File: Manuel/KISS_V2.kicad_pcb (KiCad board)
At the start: 4 copper layers, 127.4 x 127.4 mm, 73 parts, among them J1 Screw_Terminal_01x03, J2 Screw_Terminal_01x02, J3 Screw_Terminal_01x02, J5 Screw_Terminal_01x02, Q1 BC817, U1 MQ-6, U2 ULN2003, U3 AMS1117-3.3, U4 AMS1117-5.0, U5 ULN2003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

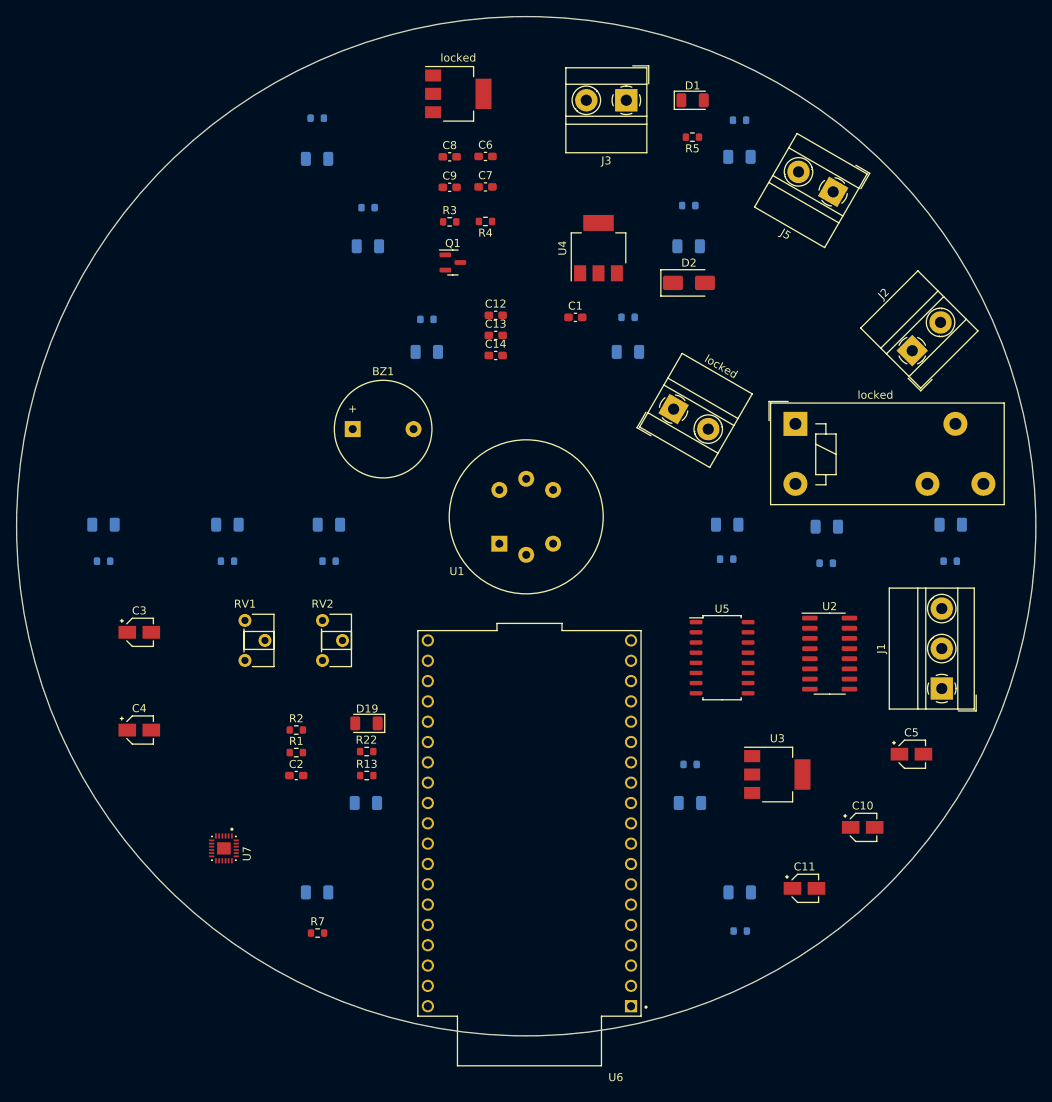
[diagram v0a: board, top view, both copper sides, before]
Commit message: Proyecto Kiss V2
Esquemático y PCB terminados
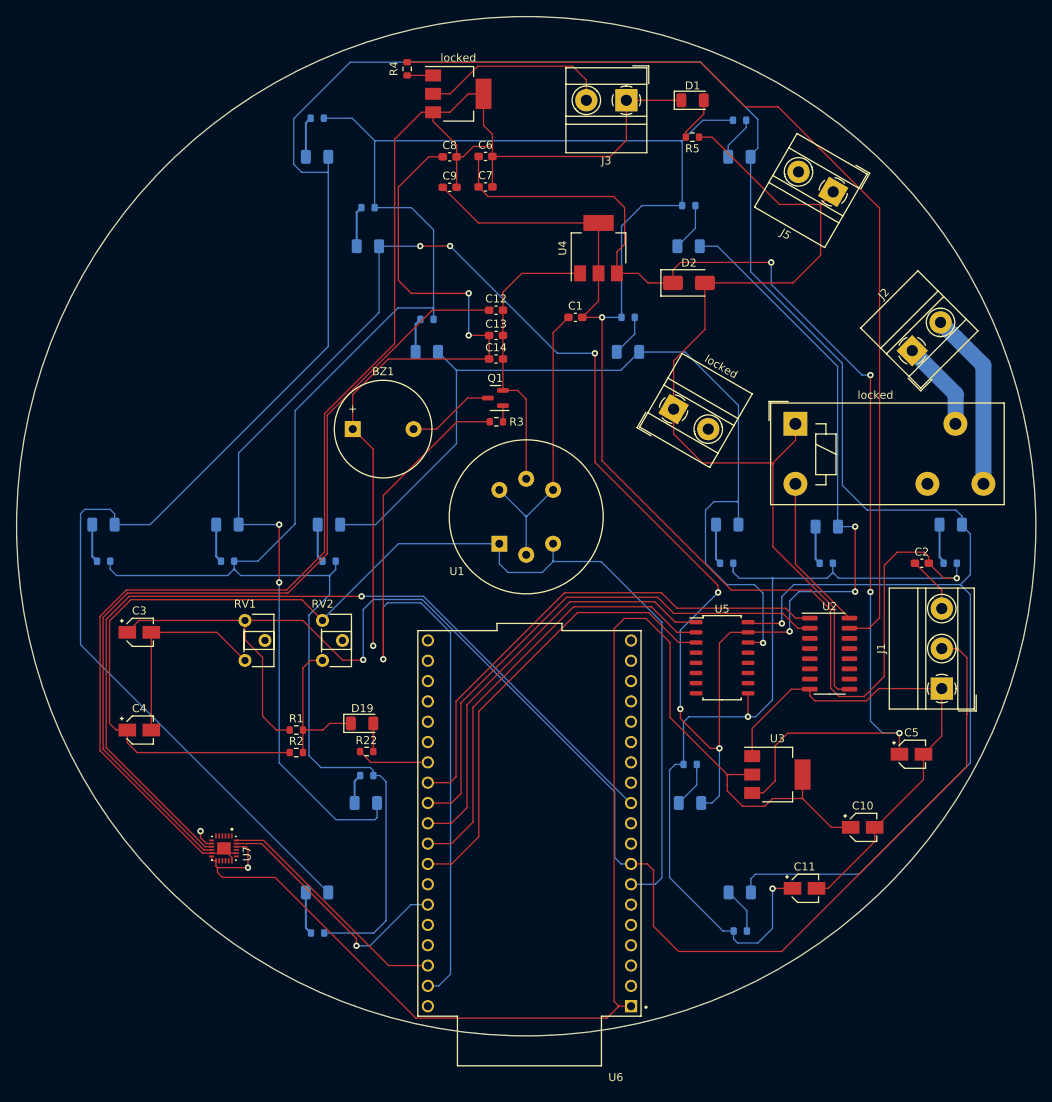
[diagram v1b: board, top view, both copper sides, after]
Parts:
- R13, R7: moved to B.Cu
- RV1, RV2: value 60K -> 20K
- moved R10 96.7 mm to (76.3, 98.0)
- moved D7 91.8 mm to (76.2, 93.4)
- moved R7 91.6 mm to (182.1, 98.2), turned to 180 degrees
- moved D4 91.6 mm to (182.2, 93.4)
- moved C2 82.6 mm to (178.5, 98.2)
- moved D15 78.0 mm to (154.2, 93.4)
- moved R18 77.9 mm to (154.1, 98.2)
- moved D18 77.7 mm to (104.4, 93.4)
- moved R21 77.6 mm to (104.5, 98.0)
- moved R8 75.3 mm to (155.8, 42.8), turned to 0 degrees
- moved R14 72.8 mm to (149.4, 53.5), turned to 0 degrees
- moved R16 72.8 mm to (91.8, 98.0)
- moved R11 69.3 mm to (103.0, 144.4)
- moved D5 68.9 mm to (155.7, 47.4)
- moved D8 68.9 mm to (102.9, 139.4)
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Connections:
- U5 pad 1: /Controlador/Pin_Activador_LEDr -> /Controlador/Pin_Activador_LEDam
- U5 pad 3: /Controlador/Pin_Activador_LEDam -> /Controlador/Pin_Activador_LEDr
- U6 pad 27: /Controlador/Modulo de Diodos/EN_D2 -> /Controlador/Modulo de Diodos/EN_D1
- U6 pad 28: /Controlador/Modulo de Diodos/EN_D1 -> /Controlador/Modulo de Diodos/EN_D2
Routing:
- net 5V: track 0.00 -> 496.6 mm, vias 0 -> 4
- net Net-(D3-K): track 0.00 -> 366.0 mm, vias 0 -> 1
- net Earth: track 0.00 -> 343.9 mm
- net Net-(D10-K): track 0.00 -> 284.6 mm, vias 0 -> 11
- net 3.3V: track 0.00 -> 265.6 mm, vias 0 -> 5
- net /Controlador/Pin_Sensor_GasEx: track 0.00 -> 185.4 mm, vias 0 -> 1
- net /Controlador/Pin_Sensor_Gas: track 0.00 -> 158.2 mm
- net Net-(D2-K): track 0.00 -> 147.6 mm, vias 0 -> 4
- net Activador de transistor: track 0.00 -> 122.1 mm
- net Positivo de bateria: track 0.00 -> 117.1 mm
- net Net-(D15-K): track 0.00 -> 113.6 mm, vias 0 -> 1
- net /Controlador/Salida_Giroscopio: track 0.00 -> 111.8 mm, vias 0 -> 1
- net Net-(U7-REGOUT): track 0.00 -> 109.6 mm
- net /Buzzer/Activador del buzzer: track 0.00 -> 100.3 mm, vias 0 -> 1
- net /Controlador/Modulo de Diodos/EN_D2: track 0.00 -> 66.7 mm
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
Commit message: PCB
PCB corregido
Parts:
- moved C12 65.8 mm to (91.3, 123.0)
- moved C13 65.8 mm to (91.3, 126.1)
- moved C14 65.8 mm to (91.3, 129.1)
- moved D10 2.15 mm to (168.8, 93.6)
- moved R13 1.64 mm to (168.2, 98.2)
- moved U1 1.16 mm to (125.5, 96.9)
- moved C3 1.16 mm to (79.6, 106.8)
- moved C4 1.16 mm to (79.6, 119.0)
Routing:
- net Net-(U7-REGOUT): track 109.6 -> 17.6 mm, vias 0 -> 2
- net Earth: track 343.9 -> 370.8 mm
- net 3.3V: track 265.6 -> 251.8 mm, vias 5 -> 3
- net Net-(D3-K): track 366.0 -> 373.5 mm
- net /Controlador/Pin_Sensor_Gas: track 158.2 -> 163.2 mm
- net Net-(D2-K): track 147.6 -> 152.3 mm
- net /Controlador/Salida_Giroscopio: track 111.8 -> 116.1 mm
- net Net-(D10-K): track 284.6 -> 287.8 mm
- net Net-(U1-A1): track 36.9 -> 38.4 mm
- net /Controlador/Pin_Sensor_GasEx: track 185.4 -> 186.5 mm
- net 5V: track 496.6 -> 497.5 mm
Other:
- outline, holes or cut-outs redrawn
